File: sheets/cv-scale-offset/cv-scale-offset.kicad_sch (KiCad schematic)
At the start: 5 parts, among them U1 TL072IP

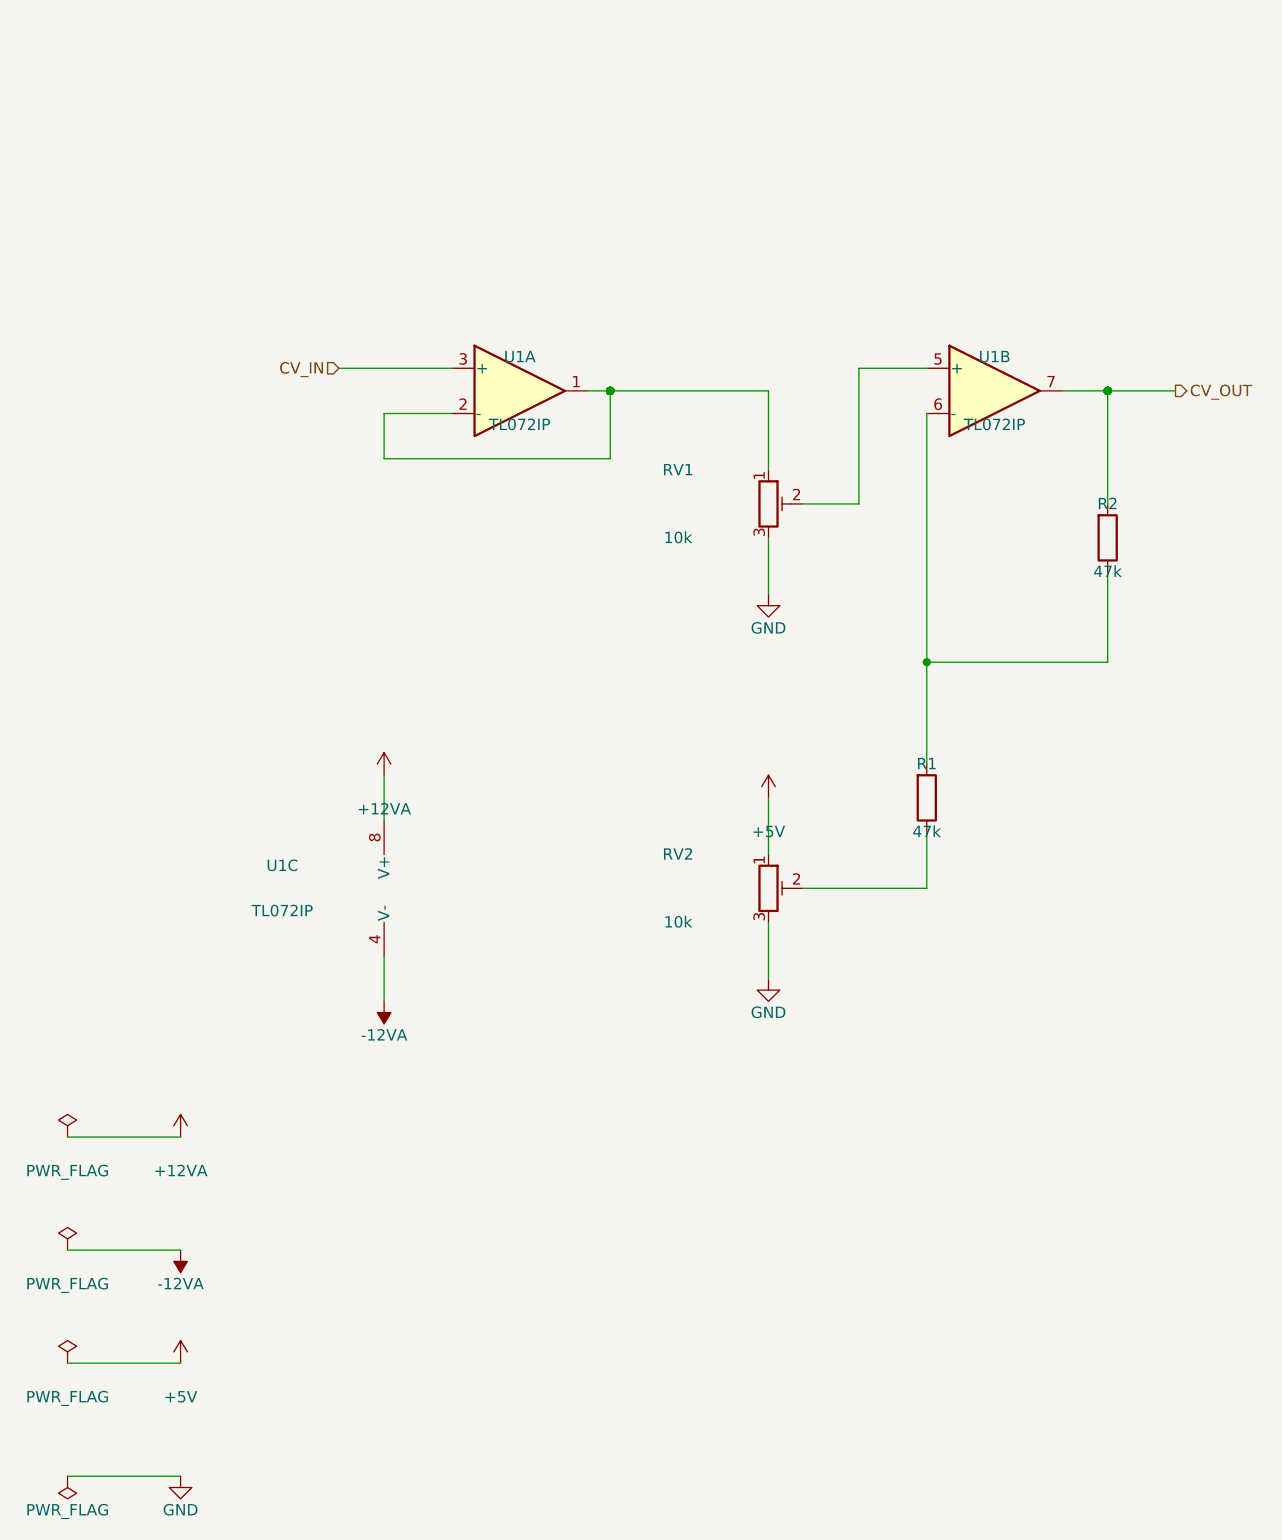
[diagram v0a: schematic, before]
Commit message: Decouple every supply pin
Each integrated circuit now has a 100nF ceramic across its supply pins,
one per package and one per rail for a split supply. Nine capacitors
across five blocks. Home boards are two layers with no ground plane, so
nothing else holds the rail up during a switching edge.

cv-output gains GND as an interface net. It had no ground reference at
all before, being a buffer between the two analogue rails, so the
decoupling brought one in and the harness needed a PWR_FLAG for it.

clock-input 1.1.1, cv-output 1.1.1, step-counter 1.0.1, cv-mux-8 1.0.1,
cv-scale-offset 1.0.1. No circuit change in any of them.

Recorded as a convention in the repo README, next to the footprint and
hierarchical label rules. ERC checks none of these three.

All nine blocks: ERC 0 errors, no overlaps.

Co-Authored-By: Claude Opus 5 (1M context) <noreply@anthropic.com>
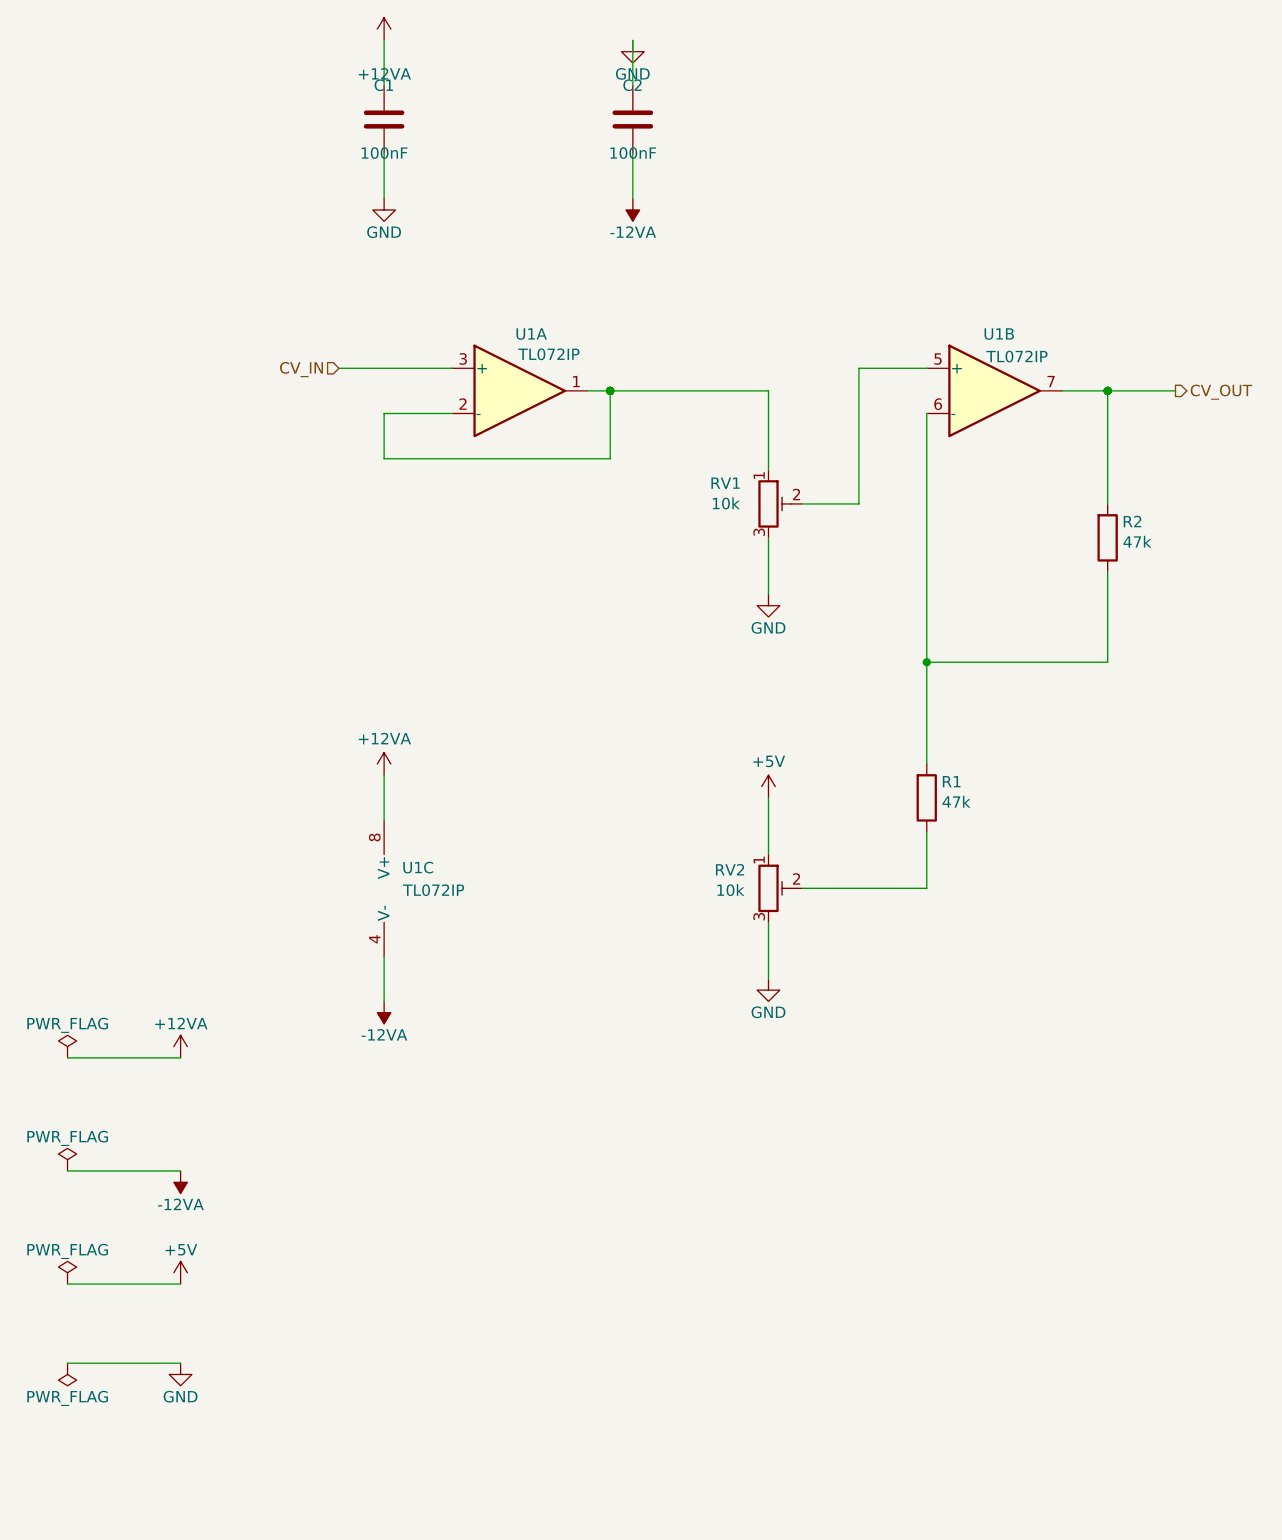
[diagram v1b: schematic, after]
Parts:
- added C1, C2: 100nF, Eurorack Common:C_Disc_D3.4mm_W2.1mm_P2.50mm, symbol Eurorack Common:C_100nF_50V_X7R_2.5mm
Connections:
- net +12VA: now also C1.1
- net -12VA: now also C2.2
- net GND: now also C1.2, C2.1
